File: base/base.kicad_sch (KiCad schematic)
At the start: 1 part, among them U1 ESP32-WROOM-32

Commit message: add base pcb
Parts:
- added C1, C2, C3, C4: C, Capacitor_SMD:C_0603_1608Metric, symbol Device:C
- added D1, D2: WS2812B, LED_SMD:LED_WS2812B_PLCC4_5.0x5.0mm_P3.2mm, symbol LED:WS2812B
- added DWM1: DWM1000, RF_Module:DWM1000, symbol RF_Module:DWM1000
- added J1: USB_B_Micro, Connector_USB:USB_Micro-B_Molex-105017-0001, symbol Connector:USB_B_Micro
- added J2: Conn_01x06, Connector_PinHeader_2.54mm:PinHeader_1x06_P2.54mm_Vertical, symbol Connector_Generic:Conn_01x06
- added R1, R2: 10K, Resistor_SMD:R_0603_1608Metric, symbol Device:R_Small
- added SW1, SW2: SW_Push_Open, Button_Switch_SMD:SW_SPST_CK_RS282G05A3, symbol Switch:SW_Push_Open
- added U2: LM317_SOT-223, Package_TO_SOT_SMD:SOT-223-3_TabPin2, symbol Regulator_Linear:LM317_SOT-223
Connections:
- net GND: now reaches U1.1 (GND), U1.15 (GND), U1.38 (GND), U1.39 (GND)
- net GND: now also C1.2, C2.2, C3.2, C4.2, D1.3 (VSS), D2.3 (VSS), DWM1.16 (VSS), DWM1.21 (VSS), DWM1.23 (VSS), DWM1.24 (VSS), DWM1.8 (VSS), J1.5 (GND), J1.6 (Shield), J2.6 (Pin_6), SW1.1 (A), SW2.2 (B), U2.1 (ADJ)
- net VCC: now reaches U1.2 (VDD)
- net VCC: now also C2.1, C3.1, C4.1, D1.1 (VDD), D2.1 (VDD), DWM1.5 (VDDAON), DWM1.6 (VDD3V3), DWM1.7 (VDD3V3), R1.1, R2.1, U2.2 (VO)
- net at U1.25 (IO0): now also R2.2, SW2.1 (A)
- net WS_IN: now reaches U1.28 (IO17)
- net WS_IN: now also D1.4 (DIN)
- net SS: now reaches U1.29 (IO5)
- net SS: now also DWM1.17 (SPICSn)
- net at U1.3 (EN): now also R1.2, SW1.2 (B)
- net CLK: now reaches U1.30 (IO18)
- net CLK: now also DWM1.20 (SPICLK)
- net MISO: now reaches U1.31 (IO19)
- net MISO: now also DWM1.19 (SPIMISO)
- net ESP_RX: now reaches U1.34 (RXD0/IO3)
- net ESP_RX: now also J2.3 (Pin_3)
- net ESP_TX: now reaches U1.35 (TXD0/IO1)
- net ESP_TX: now also J2.2 (Pin_2)
- net MOSI: now reaches U1.37 (IO23)
- net MOSI: now also DWM1.18 (SPIMOSI)
- net DW_RST: now reaches U1.6 (IO34)
- net DW_RST: now also DWM1.3 (RSTn)
- net DW_IRQ: now reaches U1.7 (IO35)
- net DW_IRQ: now also DWM1.22 (IRQ/GPIO8)
- new net: D1.2 (DOUT), D2.4 (DIN)
- new net 5V: C1.1, J1.1 (VBUS), J2.4 (Pin_4), U2.3 (VI)
- new net CTS: J2.5 (Pin_5)
- new net RST: J2.1 (Pin_1)
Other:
- note added: "LED"
- moved on the sheet: U1

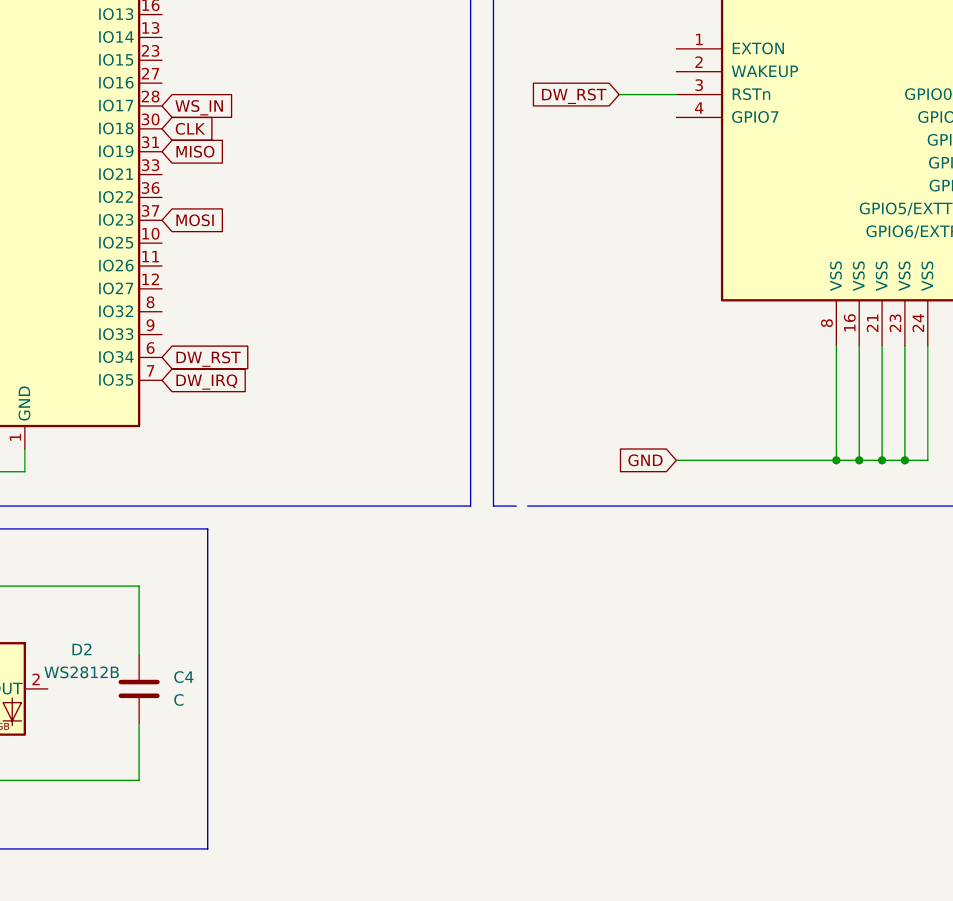
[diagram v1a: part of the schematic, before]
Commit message: add BMP280 for altimeter sensor
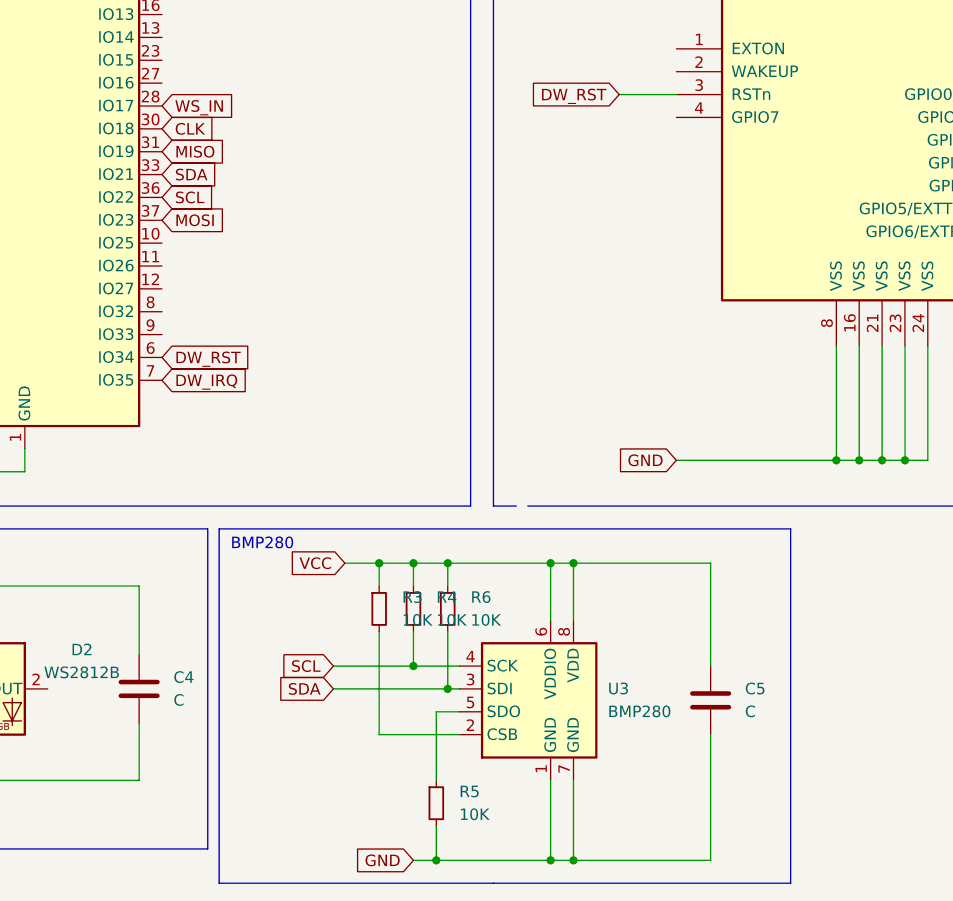
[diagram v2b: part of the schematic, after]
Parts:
- added C5: C, Capacitor_SMD:C_0603_1608Metric, symbol Device:C
- added R3, R4, R5, R6: 10K, Resistor_SMD:R_0603_1608Metric, symbol Device:R_Small
- added U3: BMP280, Package_LGA:Bosch_LGA-8_2x2.5mm_P0.65mm_ClockwisePinNumbering, symbol Sensor_Pressure:BMP280
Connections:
- net GND: now also C5.2, R5.2, U3.1 (GND), U3.7 (GND)
- net VCC: now also C5.1, R3.1, R4.1, R6.1, U3.6 (VDDIO), U3.8 (VDD)
- net SDA: now reaches U1.33 (IO21)
- net SDA: now also R6.2, U3.3 (SDI)
- net SCL: now reaches U1.36 (IO22)
- net SCL: now also R4.2, U3.4 (SCK)
- new net: R3.2, U3.2 (CSB)
- new net: R5.1, U3.5 (SDO)
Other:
- note added: "BMP280"

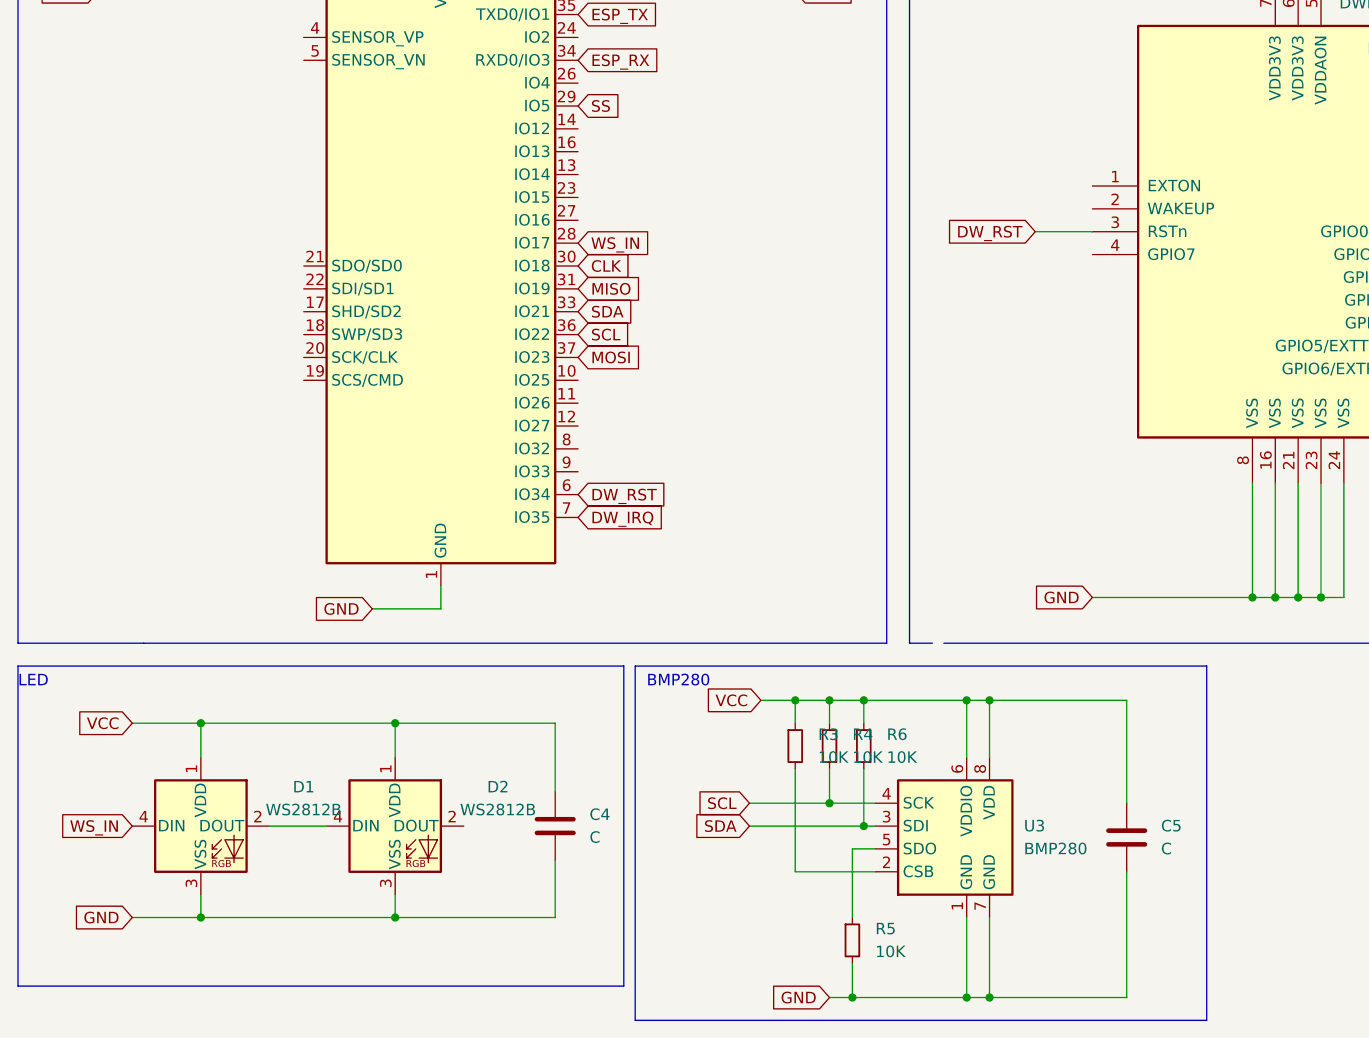
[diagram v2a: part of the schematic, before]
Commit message: change rst dw1000 pin
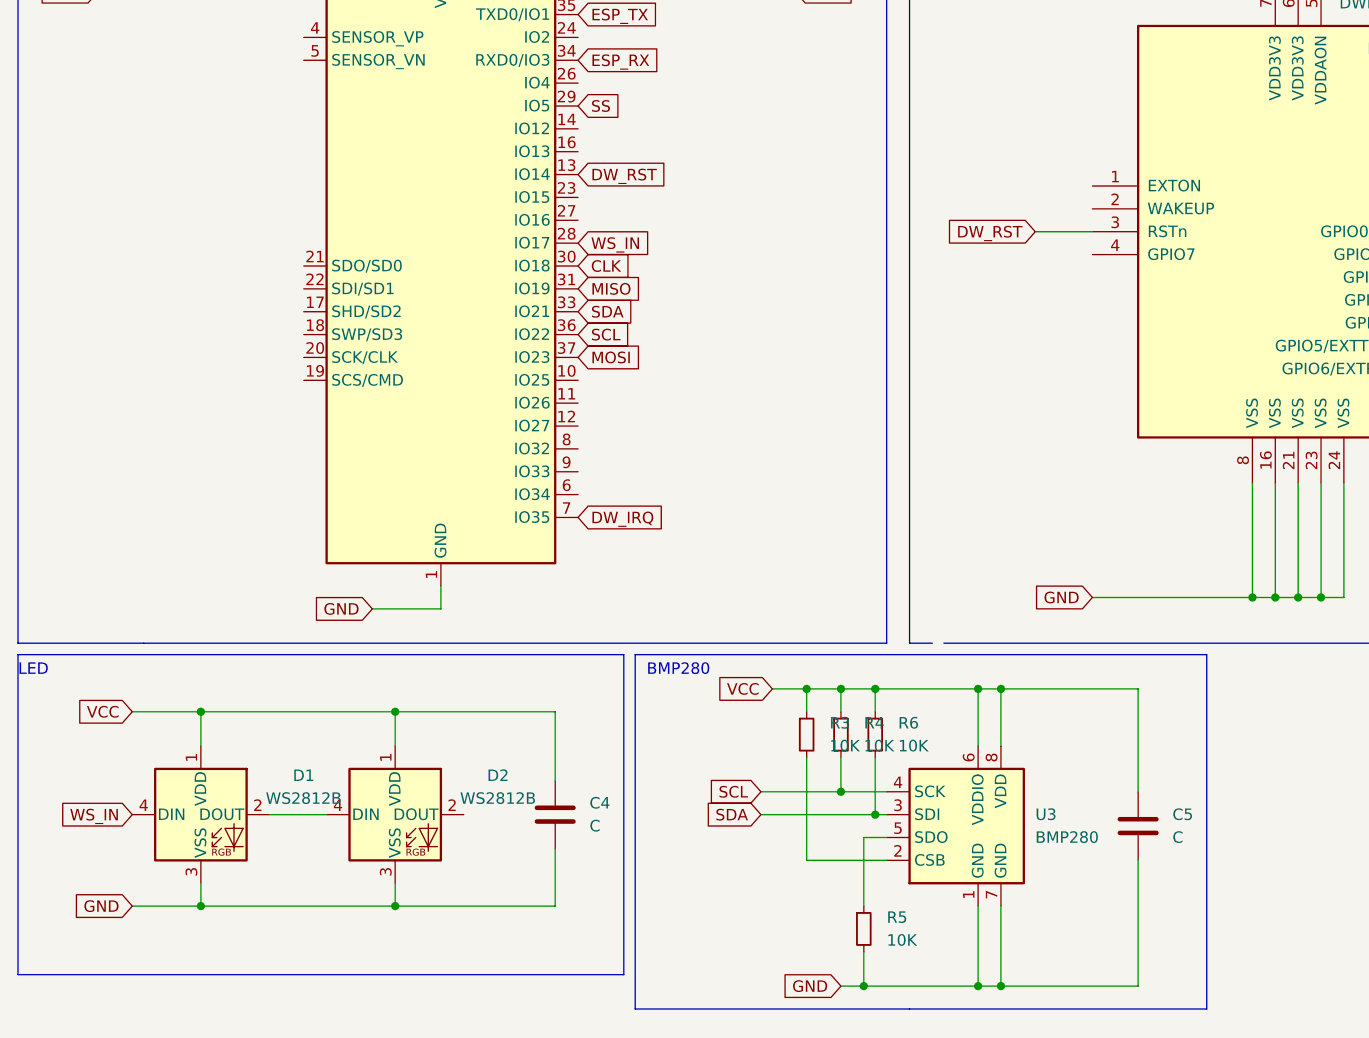
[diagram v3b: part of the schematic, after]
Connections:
- net DW_RST: now also U1.13 (IO14); no longer U1.6 (IO34)
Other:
- moved on the sheet: C4, C5, D1, D2, R3, R4, R5, R6, U3

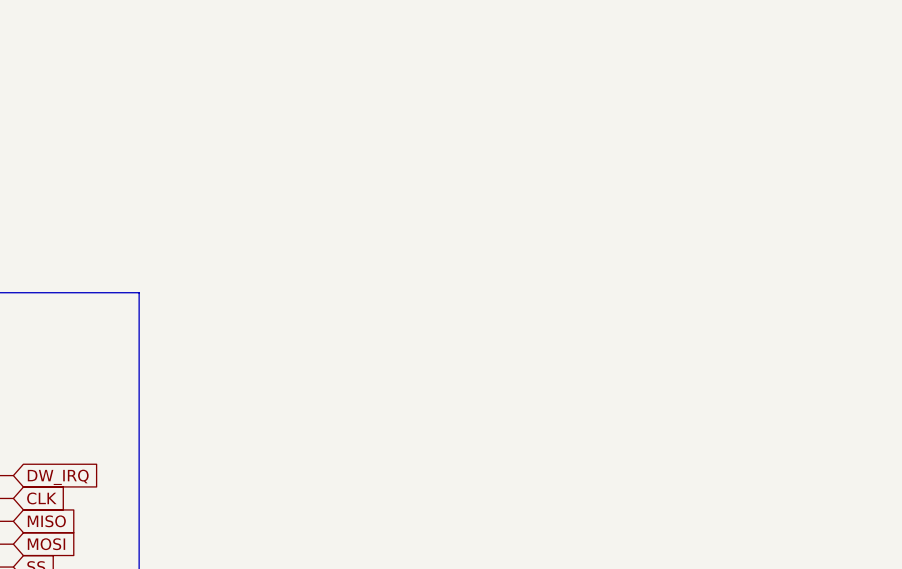
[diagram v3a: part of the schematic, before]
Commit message: add tps63001 on base
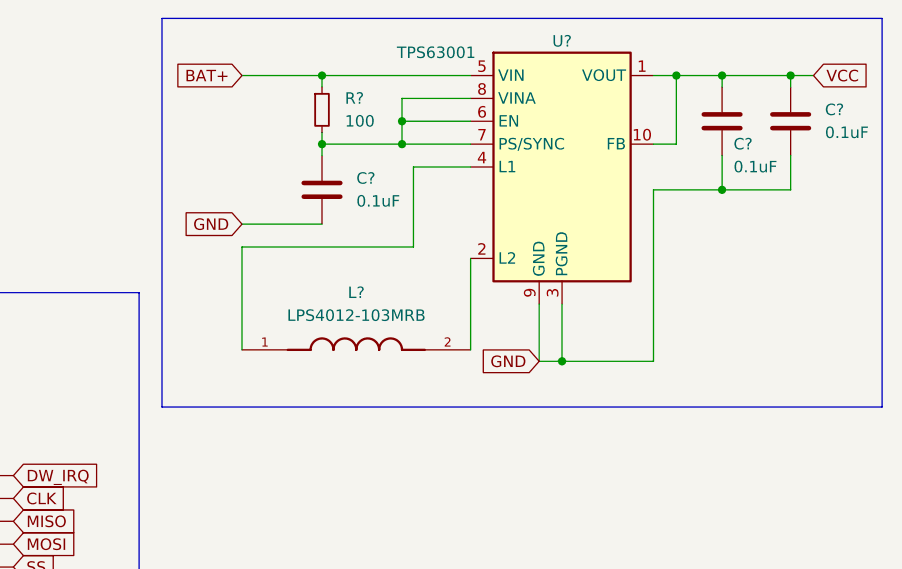
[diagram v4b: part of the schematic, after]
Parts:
- added C? (x3): 0.1uF, Capacitor_SMD:C_0603_1608Metric, symbol Device:C
- added L?: LPS4012-103MRB, LPS4012:IND_LPS4012-103MRB, symbol LPS4012:LPS4012-103MRB
- added R?: 100, Resistor_SMD:R_0603_1608Metric, symbol Device:R_Small
- added U?: TPS63001, Package_SON:Texas_DRC0010J_ThermalVias, symbol Regulator_Switching:TPS63000
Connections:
- net GND: now also C?.2, C?.2, C?.2, U?.11 (PGND), U?.3 (PGND), U?.9 (GND)
- net VCC: now also C?.1, C?.1, U?.1 (VOUT), U?.10 (FB)
- new net: C?.1, R?.2, U?.6 (EN), U?.7 (PS/SYNC), U?.8 (VINA)
- new net: L?.2, U?.2 (L2)
- new net: L?.1, U?.4 (L1)
- new net BAT+: R?.1, U?.5 (VIN)

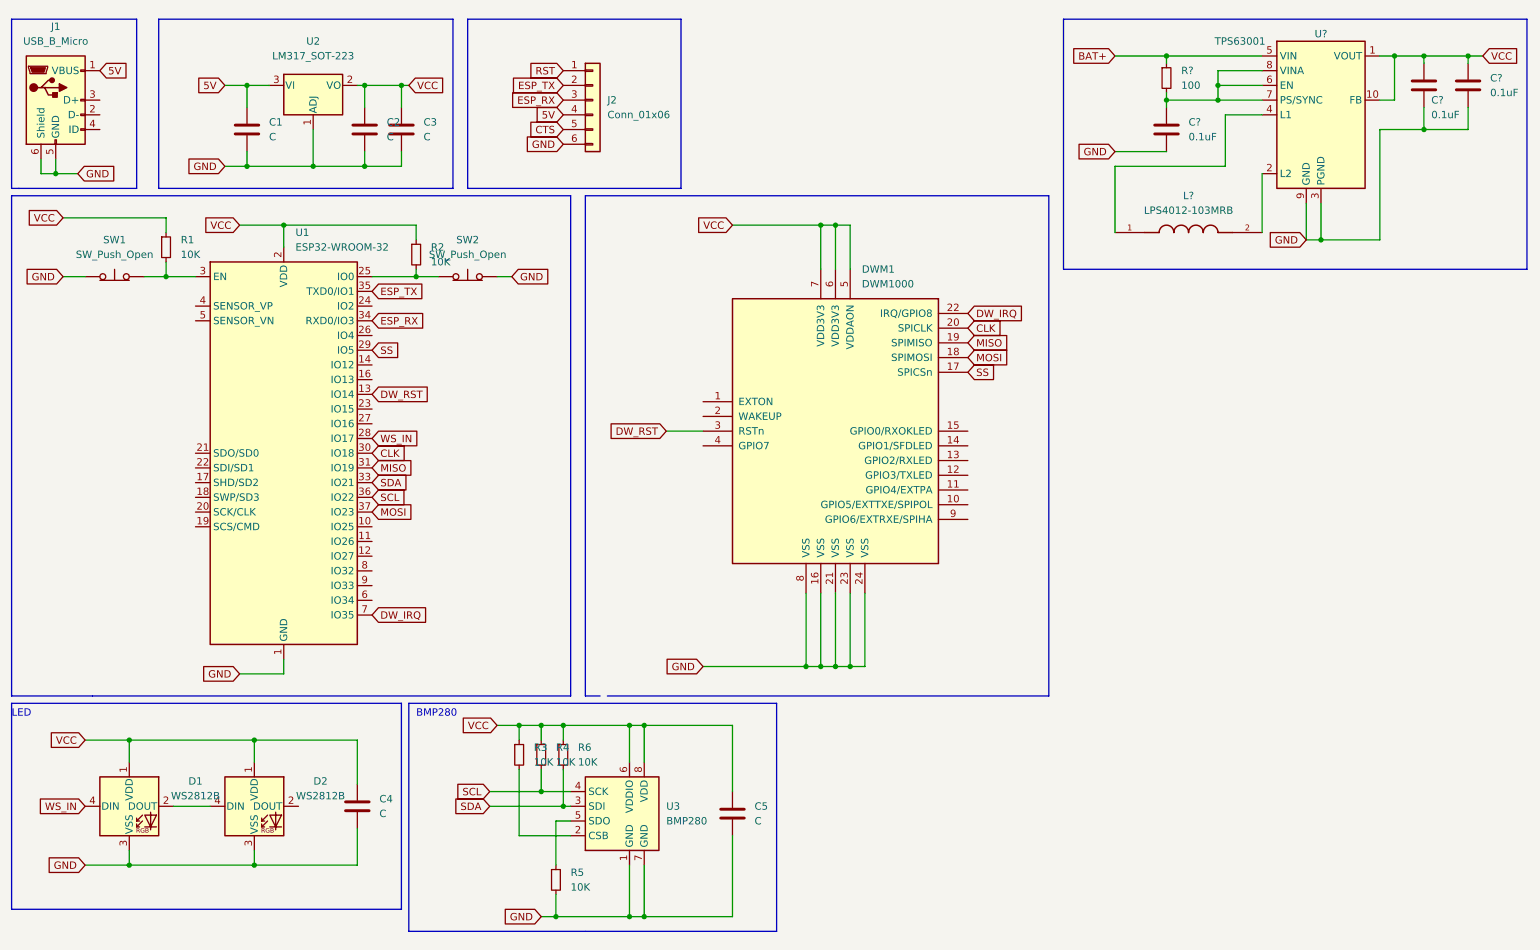
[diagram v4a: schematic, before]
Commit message: add mcp73831 on base
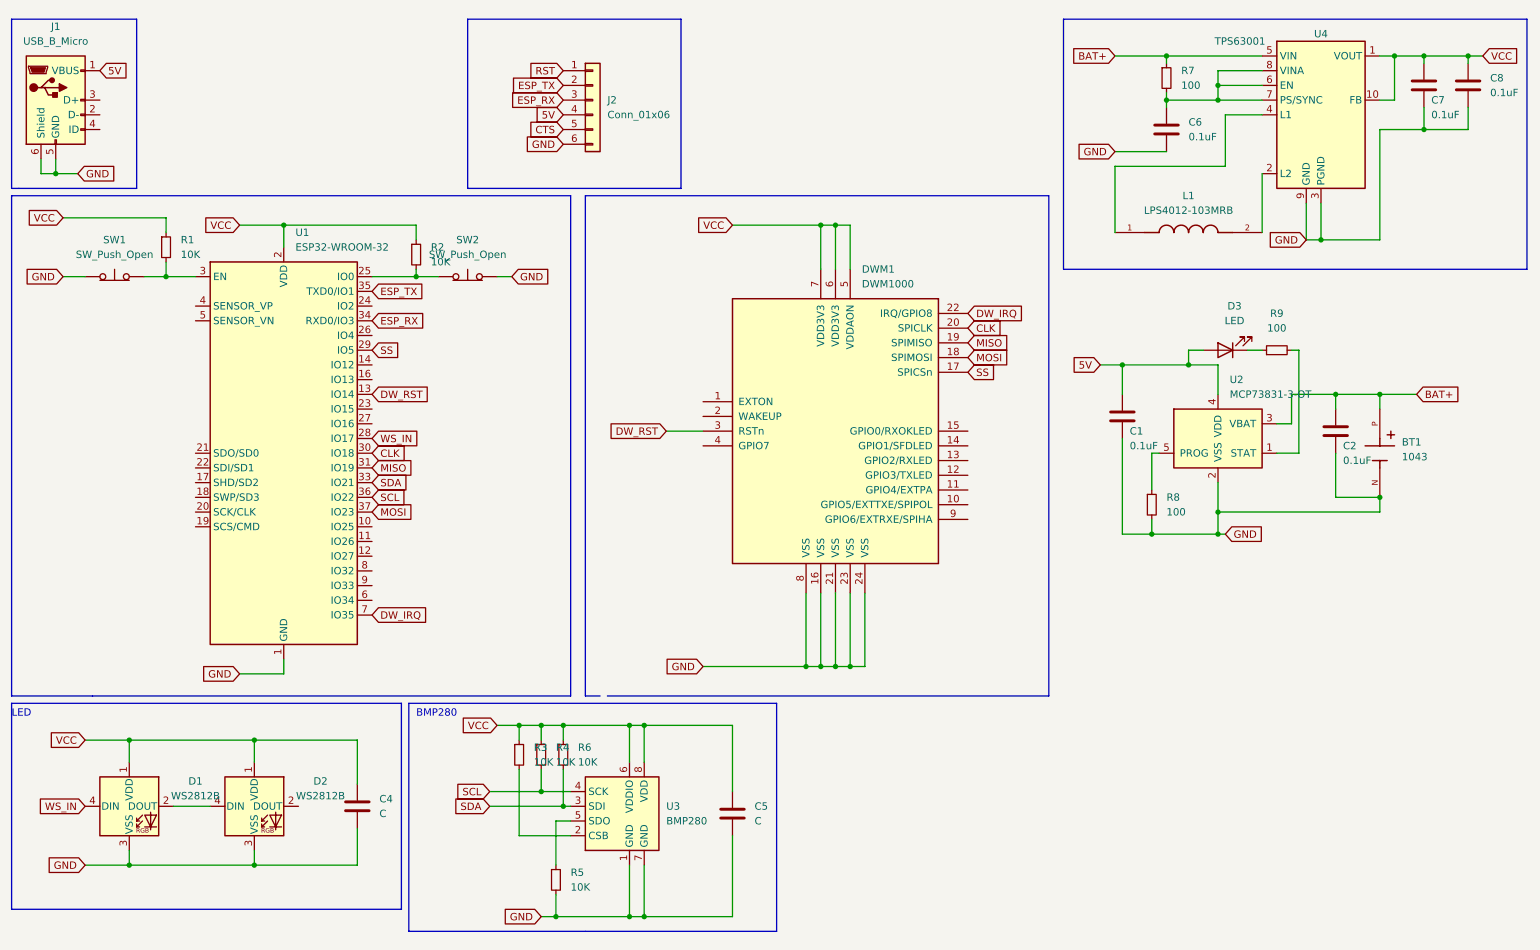
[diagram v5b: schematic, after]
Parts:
- removed C3: C, Capacitor_SMD:C_0603_1608Metric, symbol Device:C
- removed U2: LM317_SOT-223, Package_TO_SOT_SMD:SOT-223-3_TabPin2, symbol Regulator_Linear:LM317_SOT-223
- added BT1: 1043, 18650:BAT_1043, symbol 18650:1043
- added D3: LED, LED_SMD:LED_0603_1608Metric, symbol Device:LED
- added R8, R9: 100, Resistor_SMD:R_0603_1608Metric, symbol Device:R_Small
- added U2: MCP73831-3-OT, Package_TO_SOT_SMD:SOT-23-5, symbol Battery_Management:MCP73831-3-OT
- C1, C2: value C -> 0.1uF
- gave numbers to parts that had none: 6
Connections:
- net 5V: now also D3.2 (A), U2.4 (VDD)
- net BAT+: now also C2.1, BT1.P, U2.3 (VBAT)
- net GND: now also BT1.N, R8.2, U2.2 (VSS)
- net VCC: no longer C2.1
- new net: R9.2, U2.1 (STAT)
- new net: R8.1, U2.5 (PROG)
- new net: D3.1 (K), R9.1
